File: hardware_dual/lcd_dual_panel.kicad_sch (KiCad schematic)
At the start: 51 parts, among them J3 AT070TN92 FPC (0.5mm 50P, top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, Q1 AO3401A, Q2 2N7002, U7 TPS61040, U8 LM321, U9 TPS61165

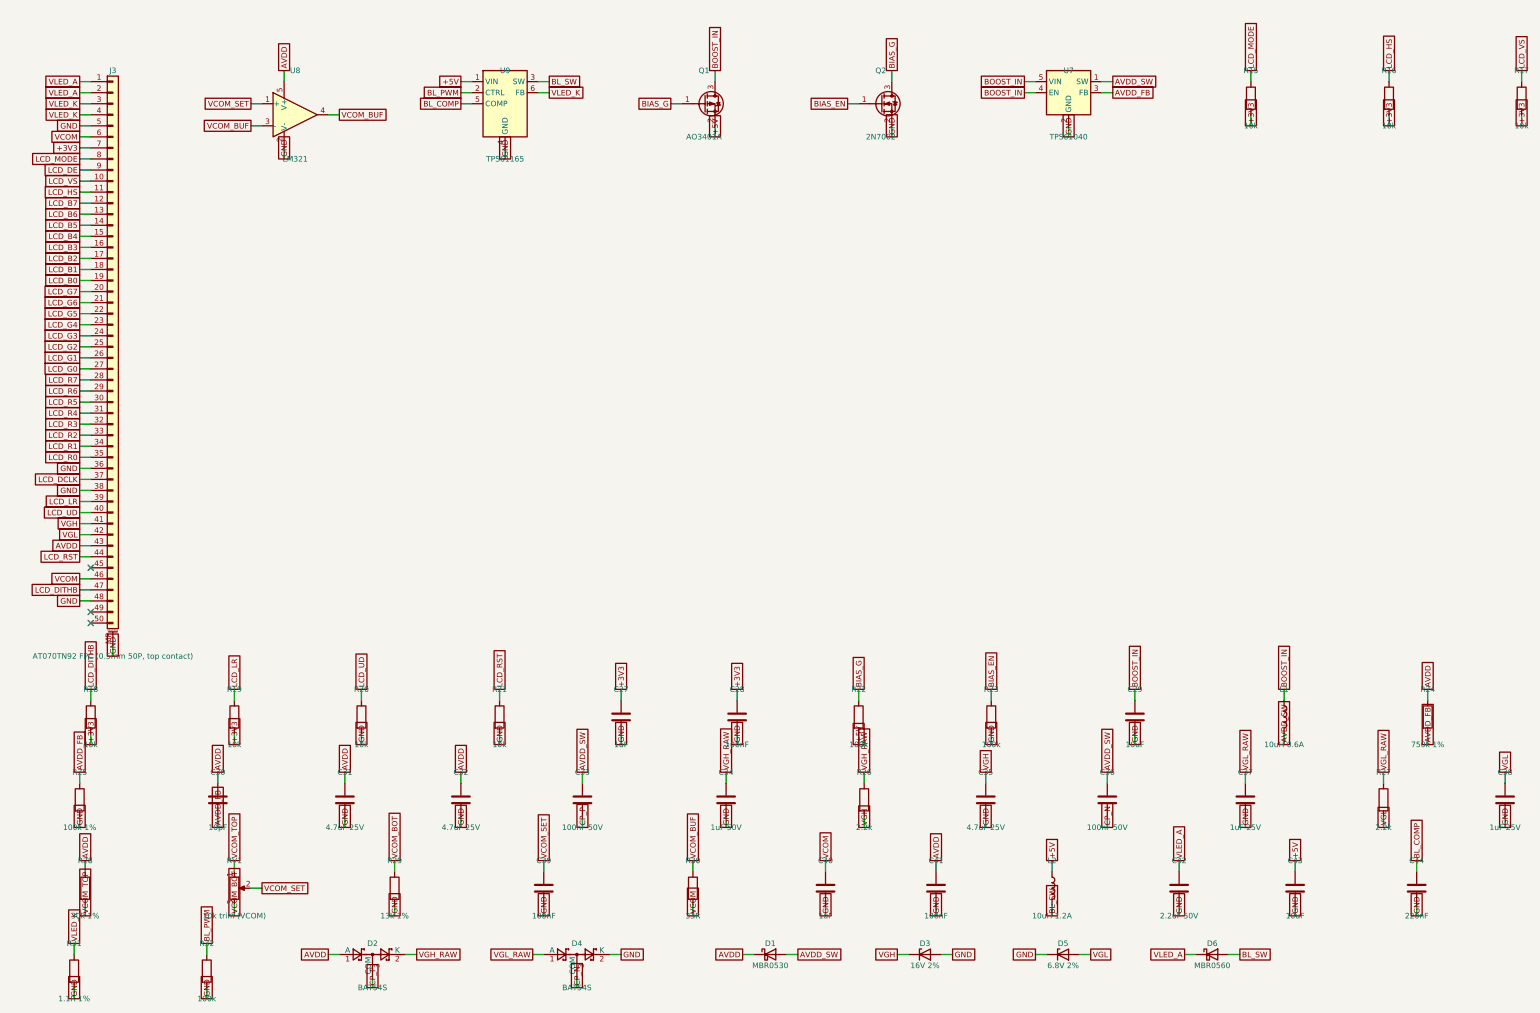
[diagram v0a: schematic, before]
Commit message: Dual board: TPS61169DCKR backlight driver
- U9 TPS61165 (SOT-23-6) -> TPS61169DCKR (SC70-5) per the TI datasheet:
  1 SW, 2 GND, 3 FB, 4 CTRL, 5 VIN; new project symbol; internal
  compensation, so C44 is removed.
- R31 1.13 R 1%: 204 mV reference -> 180 mA LED current.
- 20 kHz PWM on CTRL (datasheet 5..100 kHz), 10 uH inductor (4.7..10 uH),
  2.2 uF output capacitor (1..10 uF) are unchanged; firmware unchanged.
- Rerouted (0.7/0.4 vias): first pass plus a second pass for the last
  net (lcd_dual_stage2.ses); route.py import now prunes unused stubs.
  DRC 0 errors, 0 unconnected, netlist matches design.py.

Co-Authored-By: Claude Opus 5.5 <noreply@anthropic.com>
Claude-Session: https://claude.ai/code/session_01X8BrieHZtCS6HfoR48ML9y
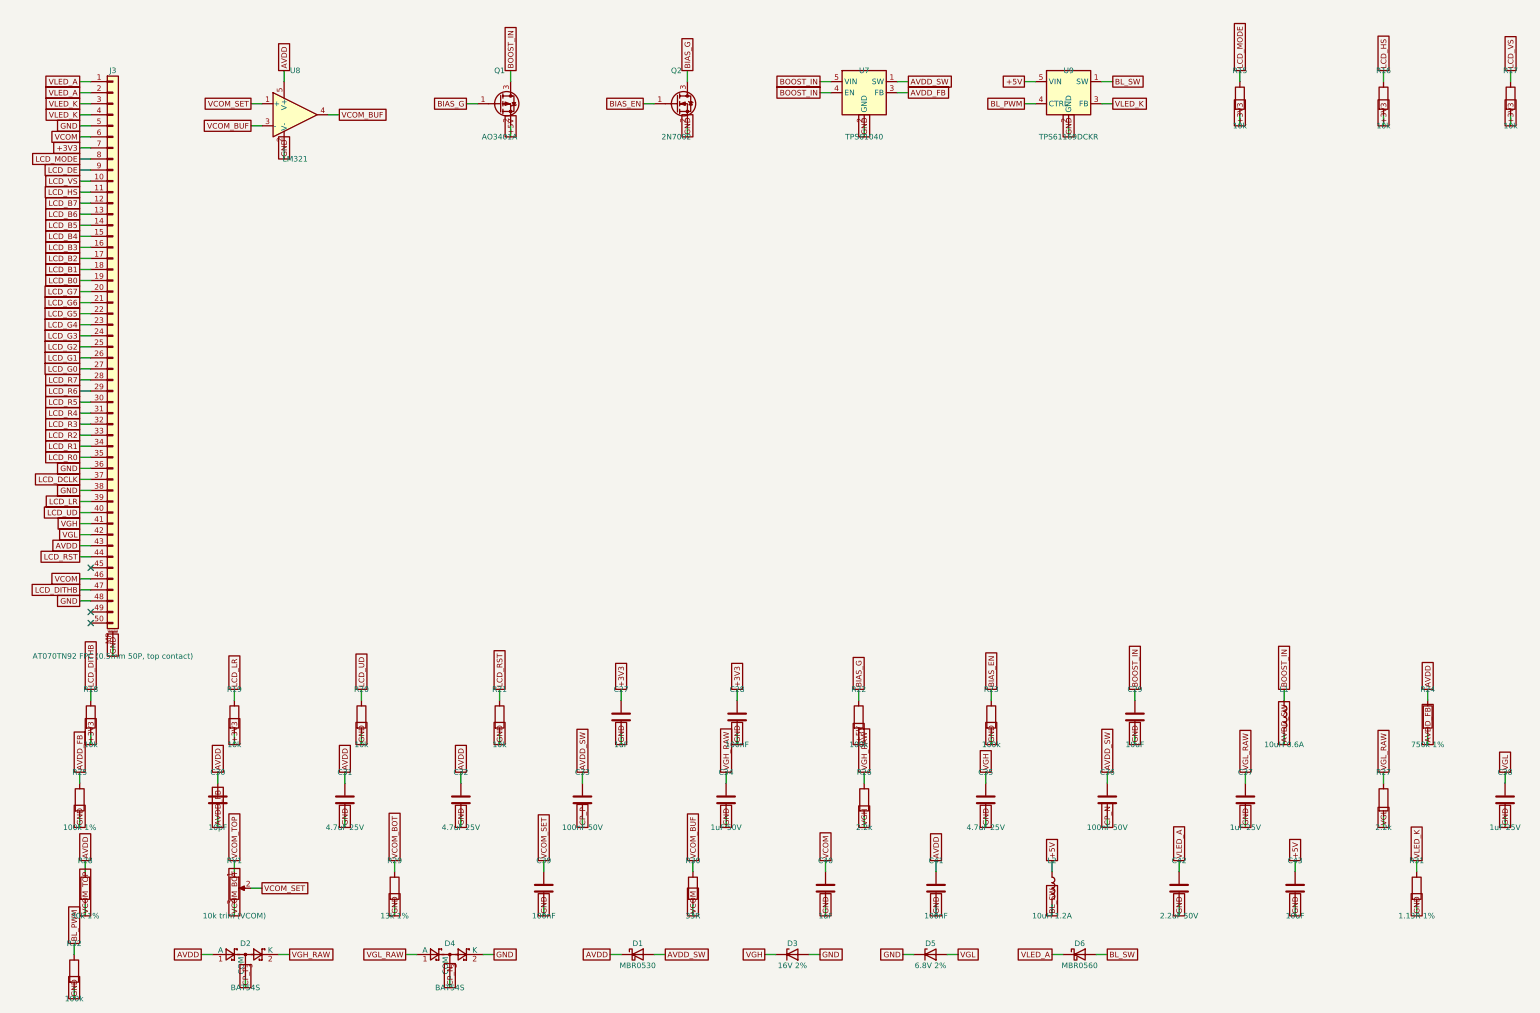
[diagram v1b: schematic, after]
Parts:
- removed C44: 220nF, Capacitor_SMD:C_0603_1608Metric, symbol Device:C
- removed U9: TPS61165, Package_TO_SOT_SMD:SOT-23-6, symbol Driver_LED:TPS61165DBV
- added U9: TPS61169DCKR, Package_TO_SOT_SMD:SOT-353_SC-70-5, symbol lcd_dual:TPS61169
- R31: value 1.1R 1% -> 1.13R 1%
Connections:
- net +5V: now also U9.5 (VIN)
- net BL_PWM: now also U9.4 (CTRL)
- net BL_SW: now also U9.1 (SW)
- net GND: now also U9.2 (GND)
- net VLED_K: now also U9.3 (FB)

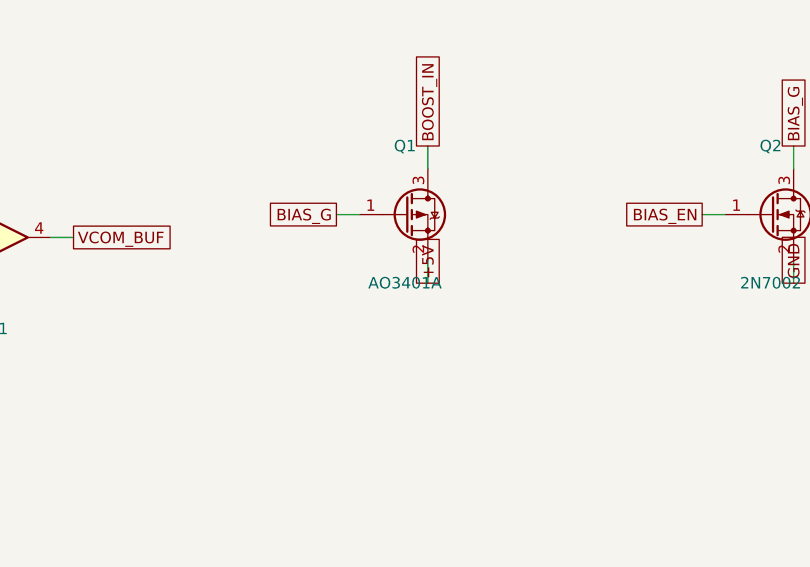
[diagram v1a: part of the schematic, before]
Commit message: Dual board: Q1 AO3401A -> AO3415
Checked against the AOS AO3415 datasheet (Rev 7): -20 V VDS, +/-8 V VGS
(the gate only sees 0 / -5 V), RDS(on) < 41 mOhm at -4.5 V, same SOT-23
pinout (1 G, 2 S, 3 D). Footprint and routing unchanged; schematic
and BOM updated (the AO3401A LCSC number is dropped).

Co-Authored-By: Claude Opus 5.5 <noreply@anthropic.com>
Claude-Session: https://claude.ai/code/session_01X8BrieHZtCS6HfoR48ML9y
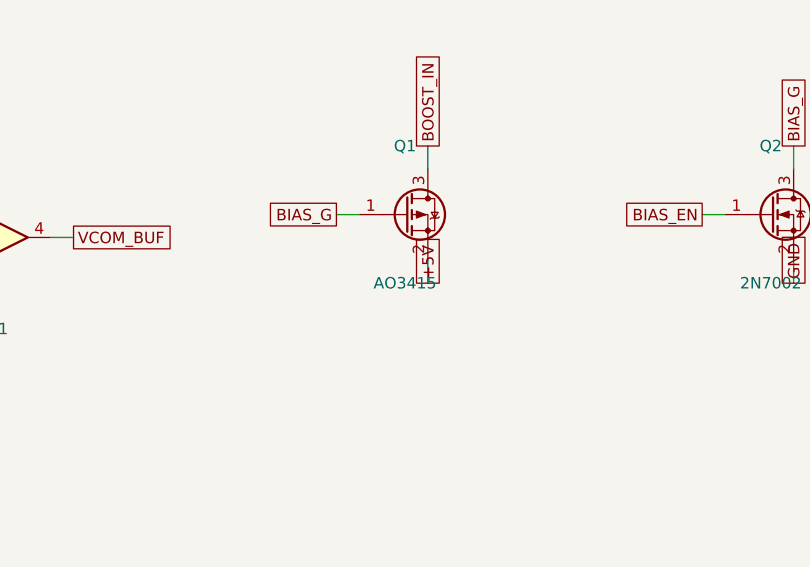
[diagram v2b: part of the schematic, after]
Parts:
- Q1: value AO3401A -> AO3415; LCSC C15127 -> (none); MPN AO3401A -> AO3415
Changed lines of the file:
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@@
         (font
           (size 1.27 1.27))))
-    (property "Value" "AO3401A"
+    (property "Value" "AO3415"
       (at 124.46 48.26 0)
       (effects
@@
         (font
           (size 1.27 1.27)) hide))
-    (property "MPN" "AO3401A"
+    (property "MPN" "AO3415"
       (at 124.46 40.64 0)
       (effects
         (font
           (size 1.27 1.27)) hide))
-    (property "LCSC" "C15127"
+    (property "LCSC" ""
       (at 124.46 40.64 0)
       (effects
